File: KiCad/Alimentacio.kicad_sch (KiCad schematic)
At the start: 6 parts

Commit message: Solucionando problemas del esquematic
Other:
- title: edd-project-grup-dimecres-dc_d_llums -> Alimentacio
- moved on the sheet: C?, D?, J?, U?

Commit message: Capacitat DC/DC
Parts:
- added C1: C_Polarized, symbol Device:C_Polarized
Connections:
- net GND: now also C1.2
- net VBAT: now also C1.1
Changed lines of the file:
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@@
+	)
+	(junction
+		(at 60.96 40.64)
+		(diameter 0)
+		(color 0 0 0 0)
 	)
 	(junction
@@
 	(wire
 		(pts
+			(xy 60.96 48.26) (xy 60.96 57.15)
+		)
+		(stroke
+			(width 0)
+			(type default)
+		)
+	)
+	(wire
+		(pts
 			(xy 140.97 45.72) (xy 147.32 45.72)
 		)
@@
 	(wire
 		(pts
-			(xy 46.99 40.64) (xy 68.58 40.64)
+			(xy 60.96 40.64) (xy 68.58 40.64)
+		)
+		(stroke
+			(width 0)
+			(type default)
+		)
+	)
+	(wire
+		(pts
+			(xy 46.99 40.64) (xy 60.96 40.64)
 		)
 		(stroke
@@
 		)
 		(instances
+			(project "Alimentacio"
+				(path "/6b132bbb-272b-40ab-bbcf-3d5da3f07086"
+					(reference "#PWR?")
+					(unit 1)
+				)
+			)
 			(project "Grup_D_Llums"
 				(path "/88ef36bc-9439-47f2-adb5-e1da6bb8c9dd/c965bb79-4e48-4b35-b9c7-2e902c1fe9a5"
@@
 		)
 		(instances
+			(project "Alimentacio"
+				(path "/6b132bbb-272b-40ab-bbcf-3d5da3f07086"
+					(reference "U?")
+					(unit 1)
+				)
+			)
 			(project "Grup_D_Llums"
 				(path "/88ef36bc-9439-47f2-adb5-e1da6bb8c9dd/c965bb79-4e48-4b35-b9c7-2e902c1fe9a5"
@@
 		)
 		(instances
+			(project "Alimentacio"
+				(path "/6b132bbb-272b-40ab-bbcf-3d5da3f07086"
+					(reference "#PWR?")
+					(unit 1)
+				)
+			)
 			(project "Grup_D_Llums"
 				(path "/88ef36bc-9439-47f2-adb5-e1da6bb8c9dd/c965bb79-4e48-4b35-b9c7-2e902c1fe9a5"
@@
 		)
 		(instances
+			(project "Alimentacio"
+				(path "/6b132bbb-272b-40ab-bbcf-3d5da3f07086"
+					(reference "U?")
+					(unit 1)
+				)
+			)
 			(project "Grup_D_Llums"
 				(path "/88ef36bc-9439-47f2-adb5-e1da6bb8c9dd/c965bb79-4e48-4b35-b9c7-2e902c1fe9a5"
@@
 	)
 	(symbol
+		(lib_id "power:GND")
+		(at 60.96 57.15 0)
+		(unit 1)
+		(exclude_from_sim no)
+		(in_bom yes)
+		(on_board yes)
+		(dnp no)
+		(fields_autoplaced yes)
+		(property "Reference" "#PWR01"
+			(at 60.96 63.5 0)
+			(effects
+				(font
+					(size 1.27 1.27)
+				)
+				(hide yes)
+			)
+		)
+		(property "Value" "GND"
+			(at 60.96 62.23 0)
+			(effects
+				(font
+					(size 1.27 1.27)
+				)
+			)
+		)
+		(property "Footprint" ""
+			(at 60.96 57.15 0)
+			(effects
+				(font
+					(size 1.27 1.27)
+				)
+				(hide yes)
+			)
+		)
+		(property "Datasheet" ""
+			(at 60.96 57.15 0)
+			(effects
+				(font
+					(size 1.27 1.27)
+				)
+				(hide yes)
+			)
+		)
+		(property "Description" "Power symbol creates a global label with name \"GND\" , ground"
+			(at 60.96 57.15 0)
+			(effects
+				(font
+					(size 1.27 1.27)
+				)
+				(hide yes)
+			)
+		)
+		(pin "1"
+		)
+		(instances
+			(project "Alimentacio"
+				(path "/6b132bbb-272b-40ab-bbcf-3d5da3f07086"
+					(reference "#PWR01")
+					(unit 1)
+				)
+			)
+		)
+	)
+	(symbol
 		(lib_id "Device:C_US")
 		(at 147.32 49.53 0)
@@
 		)
 		(instances
+			(project "Alimentacio"
+				(path "/6b132bbb-272b-40ab-bbcf-3d5da3f07086"
+					(reference "C?")
+					(unit 1)
+				)
+			)
 			(project "Grup_D_Llums"
 				(path "/88ef36bc-9439-47f2-adb5-e1da6bb8c9dd/c965bb79-4e48-4b35-b9c7-2e902c1fe9a5"
@@
 		)
 		(instances
+			(project "Alimentacio"
+				(path "/6b132bbb-272b-40ab-bbcf-3d5da3f07086"
+					(reference "#PWR?")
+					(unit 1)
+				)
+			)
 			(project "Grup_D_Llums"
 				(path "/88ef36bc-9439-47f2-adb5-e1da6bb8c9dd/c965bb79-4e48-4b35-b9c7-2e902c1fe9a5"
@@
 		)
 		(instances
+			(project "Alimentacio"
+				(path "/6b132bbb-272b-40ab-bbcf-3d5da3f07086"
+					(reference "J?")
+					(unit 1)
+				)
+			)
 			(project "Grup_D_Llums"
 				(path "/88ef36bc-9439-47f2-adb5-e1da6bb8c9dd/c965bb79-4e48-4b35-b9c7-2e902c1fe9a5"
@@
 		)
 		(instances
+			(project "Alimentacio"
+				(path "/6b132bbb-272b-40ab-bbcf-3d5da3f07086"
+					(reference "#PWR?")
+					(unit 1)
+				)
+			)
 			(project "Grup_D_Llums"
 				(path "/88ef36bc-9439-47f2-adb5-e1da6bb8c9dd/c965bb79-4e48-4b35-b9c7-2e902c1fe9a5"
@@
 		)
 		(instances
+			(project "Alimentacio"
+				(path "/6b132bbb-272b-40ab-bbcf-3d5da3f07086"
+					(reference "#PWR?")
+					(unit 1)
+				)
+			)
 			(project "Grup_D_Llums"
 				(path "/88ef36bc-9439-47f2-adb5-e1da6bb8c9dd/c965bb79-4e48-4b35-b9c7-2e902c1fe9a5"
@@
 		)
 		(instances
+			(project "Alimentacio"
+				(path "/6b132bbb-272b-40ab-bbcf-3d5da3f07086"
+					(reference "#PWR?")
+					(unit 1)
+				)
+			)
 			(project "Grup_D_Llums"
 				(path "/88ef36bc-9439-47f2-adb5-e1da6bb8c9dd/c965bb79-4e48-4b35-b9c7-2e902c1fe9a5"
@@
 		)
 		(instances
+			(project "Alimentacio"
+				(path "/6b132bbb-272b-40ab-bbcf-3d5da3f07086"
+					(reference "D?")
+					(unit 1)
+				)
+			)
 			(project "Grup_D_Llums"
 				(path "/88ef36bc-9439-47f2-adb5-e1da6bb8c9dd/c965bb79-4e48-4b35-b9c7-2e902c1fe9a5"
@@
 	)
 	(symbol
+		(lib_id "Device:C_Polarized")
+		(at 60.96 44.45 0)
+		(unit 1)
+		(exclude_from_sim no)
+		(in_bom yes)
+		(on_board yes)
+		(dnp no)
+		(fields_autoplaced yes)
+		(property "Reference" "C1"
+			(at 64.77 42.2909 0)
+			(effects
+				(font
+					(size 1.27 1.27)
+				)
+				(justify left)
+			)
+		)
+		(property "Value" "C_Polarized"
+			(at 64.77 44.8309 0)
+			(effects
+				(font
+					(size 1.27 1.27)
+				)
+				(justify left)
+			)
+		)
+		(property "Footprint" ""
+			(at 61.9252 48.26 0)
+			(effects
+				(font
+					(size 1.27 1.27)
+				)
+				(hide yes)
+			)
+		)
+		(property "Datasheet" "~"
+			(at 60.96 44.45 0)
+			(effects
+				(font
+					(size 1.27 1.27)
+				)
+				(hide yes)
+			)
+		)
+		(property "Description" "Polarized capacitor"
+			(at 60.96 44.45 0)
+			(effects
+				(font
+					(size 1.27 1.27)
+				)
+				(hide yes)
+			)
+		)
+		(pin "2"
+		)
+		(pin "1"
+		)
+		(instances
+			(project ""
+				(path "/6b132bbb-272b-40ab-bbcf-3d5da3f07086"
+					(reference "C1")
+					(unit 1)
+				)
+			)
+		)
+	)
+	(symbol
 		(lib_id "Device:C_US")
 		(at 116.84 49.53 0)
@@
 		)
 		(instances
+			(project "Alimentacio"
+				(path "/6b132bbb-272b-40ab-bbcf-3d5da3f07086"
+					(reference "C?")
+					(unit 1)
+				)
+			)
 			(project "Grup_D_Llums"
 				(path "/88ef36bc-9439-47f2-adb5-e1da6bb8c9dd/c965bb79-4e48-4b35-b9c7-2e902c1fe9a5"
@@
 		)
 	)
+	(sheet_instances
+		(path "/"
+			(page "1")
+		)
+	)
+	(embedded_fonts no)
 )

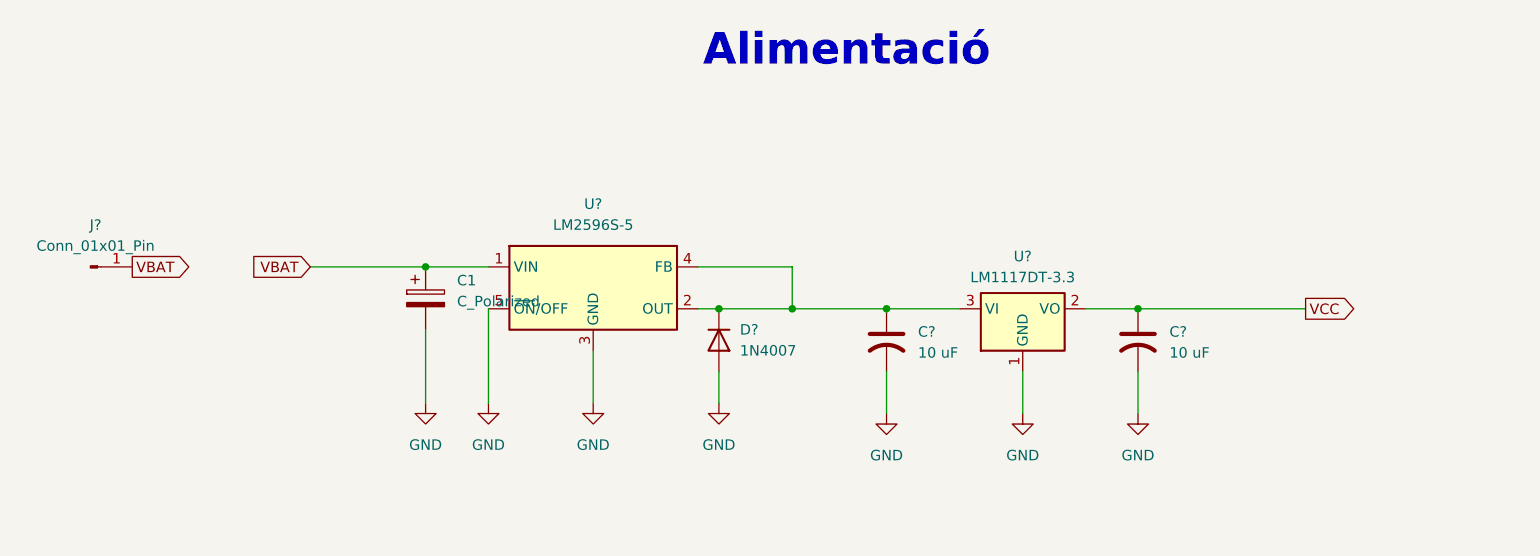
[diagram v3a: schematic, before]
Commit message: acabar can, estil y micro biel
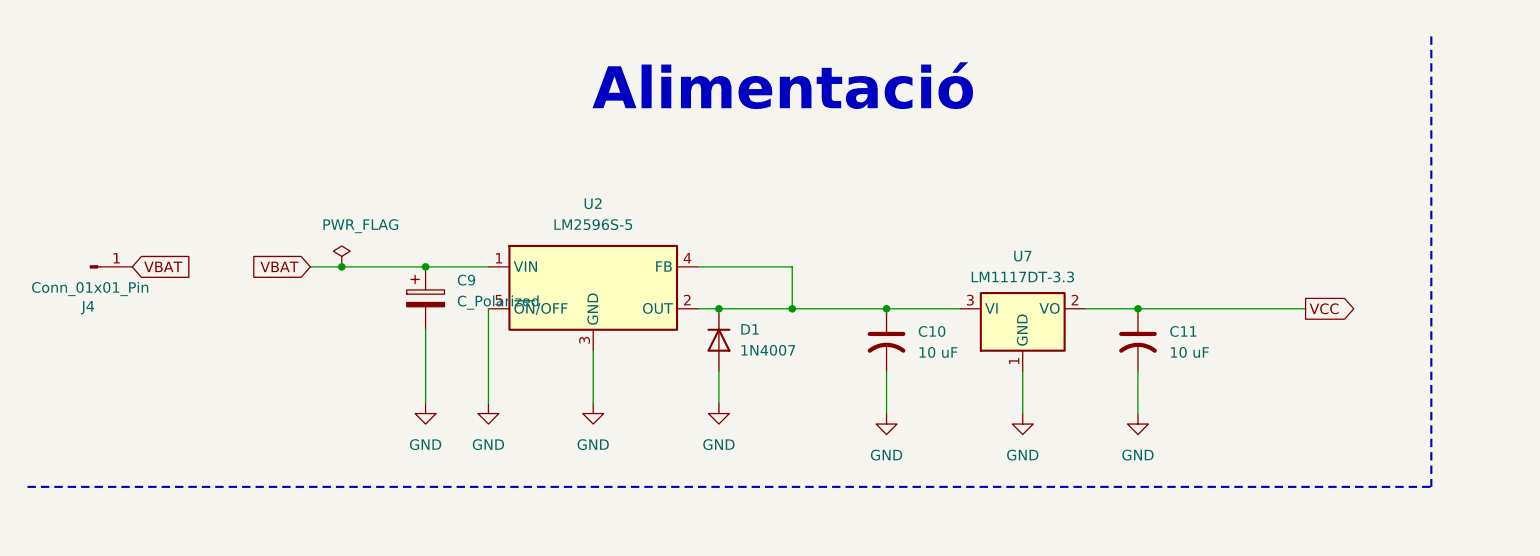
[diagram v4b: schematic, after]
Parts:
- gave numbers to parts that had none: 6
- renumbered C1 to C9
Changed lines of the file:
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@@
 	(text "Alimentació"
 		(exclude_from_sim no)
-		(at 112.014 14.478 0)
+		(at 104.394 19.304 0)
 		(effects
 			(font
-				(size 3.81 3.81)
-				(thickness 0.762)
+				(size 5.08 5.08)
+				(thickness 0.254)
 				(bold yes)
+				(color 0 0 0 1)
 			)
 		)
@@
 	)
 	(junction
+		(at 50.8 40.64)
+		(diameter 0)
+		(color 0 0 0 0)
+	)
+	(junction
 		(at 96.52 45.72)
 		(diameter 0)
@@
 	(wire
 		(pts
+			(xy 50.8 40.64) (xy 60.96 40.64)
+		)
+		(stroke
+			(width 0)
+			(type default)
+		)
+	)
+	(wire
+		(pts
 			(xy 93.98 40.64) (xy 105.41 40.64)
 		)
@@
 	(wire
 		(pts
+			(xy 105.41 45.72) (xy 116.84 45.72)
+		)
+		(stroke
+			(width 0)
+			(type default)
+		)
+	)
+	(wire
+		(pts
 			(xy 68.58 45.72) (xy 68.58 57.15)
 		)
@@
 		)
 	)
-	(wire
-		(pts
-			(xy 105.41 45.72) (xy 116.84 45.72)
-		)
-		(stroke
-			(width 0)
-			(type default)
+	(polyline
+		(pts
+			(xy 12.7 67.31) (xy 182.88 67.31)
+		)
+		(stroke
+			(width 0.254)
+			(type dash)
+			(color 0 0 0 1)
 		)
 	)
@@
 		)
 	)
-	(wire
-		(pts
-			(xy 46.99 40.64) (xy 60.96 40.64)
+	(polyline
+		(pts
+			(xy 182.88 12.7) (xy 182.88 67.31)
+		)
+		(stroke
+			(width 0.254)
+			(type dash)
+			(color 0 0 0 1)
+		)
+	)
+	(wire
+		(pts
+			(xy 46.99 40.64) (xy 50.8 40.64)
 		)
 		(stroke
@@
 	)
 	(global_label "VBAT"
-		(shape output)
+		(shape input)
 		(at 25.4 40.64 0)
 		(fields_autoplaced yes)
@@
 		(dnp no)
 		(fields_autoplaced yes)
-		(property "Reference" "#PWR?"
+		(property "Reference" "#PWR0106"
 			(at 68.58 63.5 0)
 			(effects
@@
 			(project "Grup_D_Llums"
 				(path "/88ef36bc-9439-47f2-adb5-e1da6bb8c9dd/c965bb79-4e48-4b35-b9c7-2e902c1fe9a5"
-					(reference "#PWR?")
+					(reference "#PWR0106")
+					(unit 1)
+				)
+			)
+		)
+	)
+	(symbol
+		(lib_id "power:PWR_FLAG")
+		(at 50.8 40.64 0)
+		(unit 1)
+		(exclude_from_sim no)
+		(in_bom yes)
+		(on_board yes)
+		(dnp no)
+		(property "Reference" "#FLG01"
+			(at 50.8 38.735 0)
+			(effects
+				(font
+					(size 1.27 1.27)
+				)
+				(hide yes)
+			)
+		)
+		(property "Value" "PWR_FLAG"
+			(at 53.086 35.56 0)
+			(effects
+				(font
+					(size 1.27 1.27)
+				)
+			)
+		)
+		(property "Footprint" ""
+			(at 50.8 40.64 0)
+			(effects
+				(font
+					(size 1.27 1.27)
+				)
+				(hide yes)
+			)
+		)
+		(property "Datasheet" "~"
+			(at 50.8 40.64 0)
+			(effects
+				(font
+					(size 1.27 1.27)
+				)
+				(hide yes)
+			)
+		)
+		(property "Description" "Special symbol for telling ERC where power comes from"
+			(at 50.8 40.64 0)
+			(effects
+				(font
+					(size 1.27 1.27)
+				)
+				(hide yes)
+			)
+		)
+		(pin "1"
+		)
+		(instances
+			(project ""
+				(path "/88ef36bc-9439-47f2-adb5-e1da6bb8c9dd/c965bb79-4e48-4b35-b9c7-2e902c1fe9a5"
+					(reference "#FLG01")
 					(unit 1)
 				)
@@
 		(dnp no)
 		(fields_autoplaced yes)
-		(property "Reference" "U?"
+		(property "Reference" "U2"
 			(at 81.28 33.02 0)
 			(effects
@@
 			(project "Grup_D_Llums"
 				(path "/88ef36bc-9439-47f2-adb5-e1da6bb8c9dd/c965bb79-4e48-4b35-b9c7-2e902c1fe9a5"
-					(reference "U?")
+					(reference "U2")
 					(unit 1)
 				)
@@
 		(dnp no)
 		(fields_autoplaced yes)
-		(property "Reference" "#PWR?"
+		(property "Reference" "#PWR0104"
 			(at 116.84 64.77 0)
 			(effects
@@
 			(project "Grup_D_Llums"
 				(path "/88ef36bc-9439-47f2-adb5-e1da6bb8c9dd/c965bb79-4e48-4b35-b9c7-2e902c1fe9a5"
-					(reference "#PWR?")
+					(reference "#PWR0104")
 					(unit 1)
 				)
@@
 		(dnp no)
 		(fields_autoplaced yes)
-		(property "Reference" "U?"
+		(property "Reference" "U7"
 			(at 133.35 39.37 0)
 			(effects
@@
 			(project "Grup_D_Llums"
 				(path "/88ef36bc-9439-47f2-adb5-e1da6bb8c9dd/c965bb79-4e48-4b35-b9c7-2e902c1fe9a5"
-					(reference "U?")
+					(reference "U7")
 					(unit 1)
 				)
@@
 		(dnp no)
 		(fields_autoplaced yes)
-		(property "Reference" "#PWR?"
+		(property "Reference" "#PWR0105"
 			(at 60.96 63.5 0)
 			(effects
@@
 			(project "Grup_D_Llums"
 				(path "/88ef36bc-9439-47f2-adb5-e1da6bb8c9dd/c965bb79-4e48-4b35-b9c7-2e902c1fe9a5"
-					(reference "#PWR?")
+					(reference "#PWR0105")
 					(unit 1)
 				)
@@
 		(dnp no)
 		(fields_autoplaced yes)
-		(property "Reference" "C?"
+		(property "Reference" "C11"
 			(at 151.13 48.5139 0)
 			(effects
@@
 			(project "Grup_D_Llums"
 				(path "/88ef36bc-9439-47f2-adb5-e1da6bb8c9dd/c965bb79-4e48-4b35-b9c7-2e902c1fe9a5"
-					(reference "C?")
+					(reference "C11")
 					(unit 1)
 				)
@@
 		(dnp no)
 		(fields_autoplaced yes)
-		(property "Reference" "#PWR?"
+		(property "Reference" "#PWR0102"
 			(at 147.32 64.77 0)
 			(effects
@@
 			(project "Grup_D_Llums"
 				(path "/88ef36bc-9439-47f2-adb5-e1da6bb8c9dd/c965bb79-4e48-4b35-b9c7-2e902c1fe9a5"
-					(reference "#PWR?")
+					(reference "#PWR0102")
 					(unit 1)
 				)
@@
 		(on_board yes)
 		(dnp no)
-		(fields_autoplaced yes)
-		(property "Reference" "J?"
-			(at 20.955 35.56 0)
+		(property "Reference" "J4"
+			(at 20.066 45.466 0)
 			(effects
 				(font
@@
 		)
 		(property "Value" "Conn_01x01_Pin"
-			(at 20.955 38.1 0)
+			(at 20.32 43.18 0)
 			(effects
 				(font
@@
 			(project "Grup_D_Llums"
 				(path "/88ef36bc-9439-47f2-adb5-e1da6bb8c9dd/c965bb79-4e48-4b35-b9c7-2e902c1fe9a5"
-					(reference "J?")
+					(reference "J4")
 					(unit 1)
 				)
@@
 		(dnp no)
 		(fields_autoplaced yes)
-		(property "Reference" "#PWR?"
+		(property "Reference" "#PWR0107"
 			(at 81.28 63.5 0)
 			(effects
@@
 			(project "Grup_D_Llums"
 				(path "/88ef36bc-9439-47f2-adb5-e1da6bb8c9dd/c965bb79-4e48-4b35-b9c7-2e902c1fe9a5"
-					(reference "#PWR?")
+					(reference "#PWR0107")
 					(unit 1)
 				)
@@
 		(dnp no)
 		(fields_autoplaced yes)
-		(property "Reference" "#PWR?"
+		(property "Reference" "#PWR0103"
 			(at 133.35 64.77 0)
 			(effects
@@
 			(project "Grup_D_Llums"
 				(path "/88ef36bc-9439-47f2-adb5-e1da6bb8c9dd/c965bb79-4e48-4b35-b9c7-2e902c1fe9a5"
-					(reference "#PWR?")
+					(reference "#PWR0103")
 					(unit 1)
 				)
@@
 		(dnp no)
 		(fields_autoplaced yes)
-		(property "Reference" "#PWR?"
+		(property "Reference" "#PWR0101"
 			(at 96.52 63.5 0)
 			(effects
@@
 			(project "Grup_D_Llums"
 				(path "/88ef36bc-9439-47f2-adb5-e1da6bb8c9dd/c965bb79-4e48-4b35-b9c7-2e902c1fe9a5"
-					(reference "#PWR?")
+					(reference "#PWR0101")
 					(unit 1)
 				)
@@
 		(dnp no)
 		(fields_autoplaced yes)
-		(property "Reference" "D?"
+		(property "Reference" "D1"
 			(at 99.06 48.2599 90)
 			(effects
@@
 			(project "Grup_D_Llums"
 				(path "/88ef36bc-9439-47f2-adb5-e1da6bb8c9dd/c965bb79-4e48-4b35-b9c7-2e902c1fe9a5"
-					(reference "D?")
+					(reference "D1")
 					(unit 1)
 				)
@@
 		(dnp no)
 		(fields_autoplaced yes)
-		(property "Reference" "C?"
+		(property "Reference" "C9"
 			(at 64.77 42.2909 0)
 			(effects
@@
 			(project "Grup_D_Llums"
 				(path "/88ef36bc-9439-47f2-adb5-e1da6bb8c9dd/c965bb79-4e48-4b35-b9c7-2e902c1fe9a5"
-					(reference "C?")
+					(reference "C9")
 					(unit 1)
 				)
@@
 		(dnp no)
 		(fields_autoplaced yes)
-		(property "Reference" "C?"
+		(property "Reference" "C10"
 			(at 120.65 48.5139 0)
 			(effects
@@
 			(project "Grup_D_Llums"
 				(path "/88ef36bc-9439-47f2-adb5-e1da6bb8c9dd/c965bb79-4e48-4b35-b9c7-2e902c1fe9a5"
-					(reference "C?")
-					(unit 1)
-				)
+					(reference "C10")
+					(unit 1)
+				)

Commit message: Alimentació arreglada
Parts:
- removed D1: 1N4007, Diode_THT:D_DO-41_SOD81_P10.16mm_Horizontal, symbol Diode:1N4007
- removed J4: Conn_01x01_Pin, symbol Connector:Conn_01x01_Pin
- added C1: 220 uF, symbol Device:C_Polarized
- added D1: 1N5822, Diode_THT:D_DO-201AD_P15.24mm_Horizontal, symbol Diode:1N5822
- added J3: Conn_01x02_Pin, symbol Connector:Conn_01x02_Pin
- added L1: L, symbol Device:L
- C9: value C_Polarized -> 680 uF
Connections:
- net GND: now also C1.2, D1.2 (A), J3.2 (Pin_2)
- net VBAT: now also J3.1 (Pin_1)
- net 5VOLTS: now reaches C10.1, U2.4 (FB), U7.3 (VI)
- net 5VOLTS: now also C1.1, L1.2; no longer U2.2 (OUT)
- new net: D1.1 (K), L1.1, U2.2 (OUT)
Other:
- moved on the sheet: C9
